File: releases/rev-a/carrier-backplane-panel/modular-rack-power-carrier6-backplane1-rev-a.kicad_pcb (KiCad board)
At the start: 4 copper layers, 163.8 x 237.3 mm, 723 parts

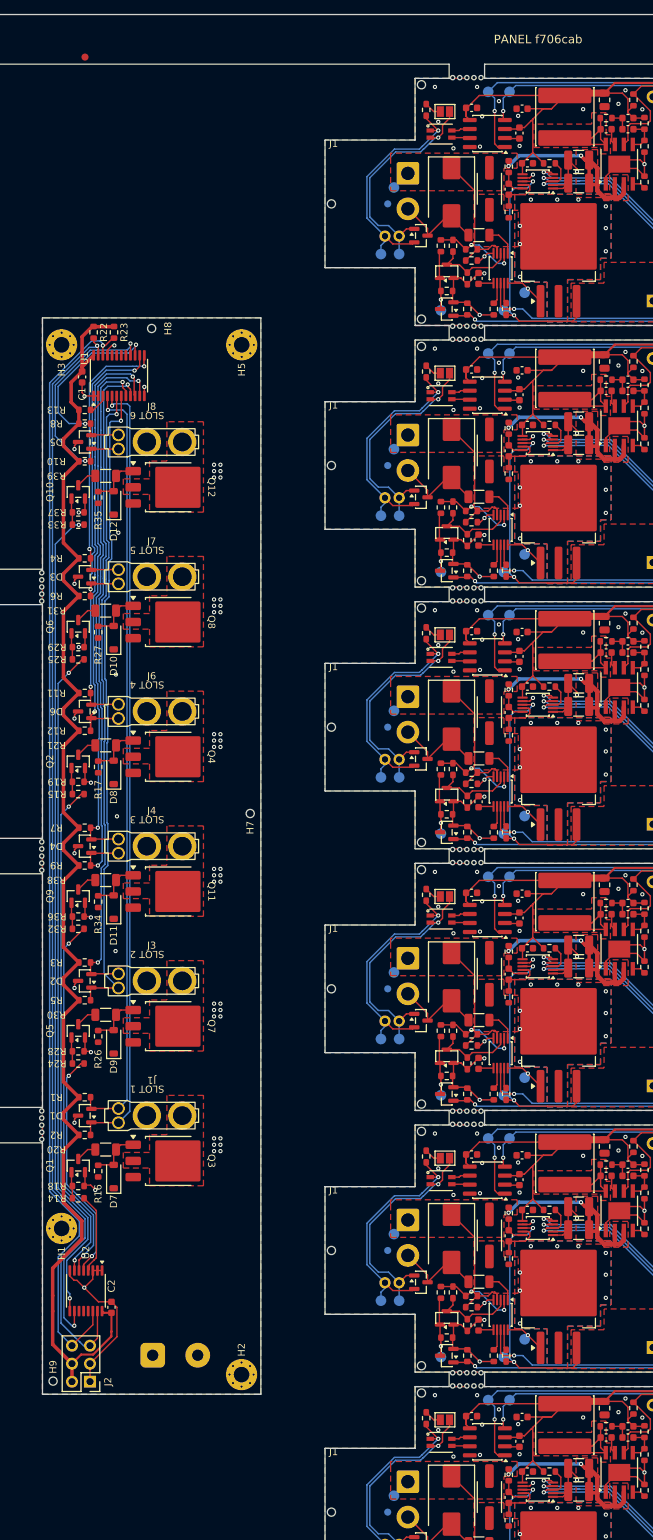
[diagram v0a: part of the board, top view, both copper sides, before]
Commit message: Gate panel builds and complete PCB renders
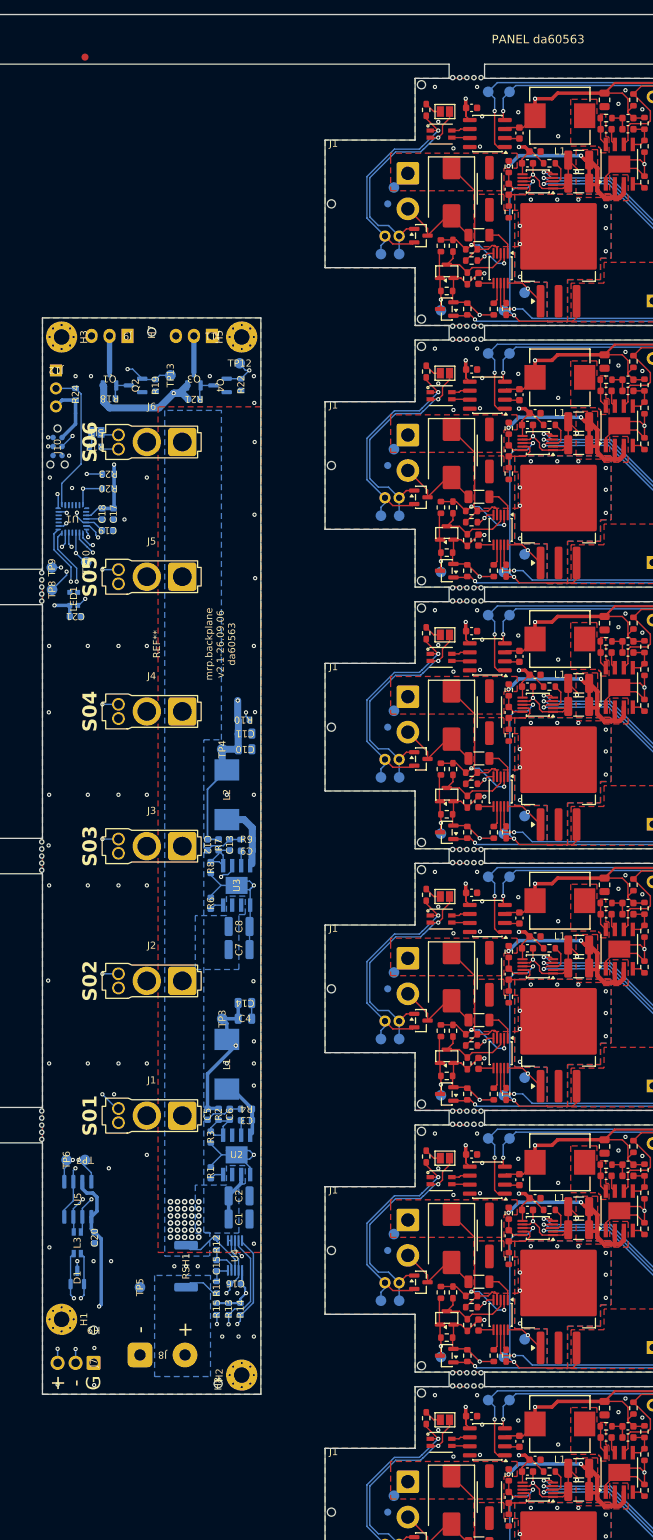
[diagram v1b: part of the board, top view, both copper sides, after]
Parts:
- removed BACKPLANE1-D10, BACKPLANE1-D11, BACKPLANE1-D12, BACKPLANE1-D7, BACKPLANE1-D8, BACKPLANE1-D9: BZT52C12-7-F, Diode_SMD:D_SOD-123
- removed BACKPLANE1-D2, BACKPLANE1-D3, BACKPLANE1-D4, BACKPLANE1-D5, BACKPLANE1-D6: PESD5V0S2BT,215, Package_TO_SOT_SMD:SOT-23
- removed BACKPLANE1-Q10, BACKPLANE1-Q5, BACKPLANE1-Q6, BACKPLANE1-Q9: BSS123, Package_TO_SOT_SMD:SOT-23
- removed BACKPLANE1-Q11, BACKPLANE1-Q12, BACKPLANE1-Q7, BACKPLANE1-Q8: SQD50P06-15L_GE3, Package_TO_SOT_SMD:TO-252-3_TabPin2
- removed BACKPLANE1-R16, BACKPLANE1-R26, BACKPLANE1-R27, BACKPLANE1-R34, BACKPLANE1-R35: 100k, Resistor_SMD:R_0603_1608Metric
- removed BACKPLANE1-R25, BACKPLANE1-R32, BACKPLANE1-R33: 1k, Resistor_SMD:R_0603_1608Metric
- removed BACKPLANE1-R28, BACKPLANE1-R29, BACKPLANE1-R36, BACKPLANE1-R37: 10k, Resistor_SMD:R_0603_1608Metric
- removed BACKPLANE1-R30, BACKPLANE1-R31, BACKPLANE1-R38, BACKPLANE1-R39: 10k, Resistor_SMD:R_1206_3216Metric
- removed BACKPLANE1-R5: 4.7k 1%, Resistor_SMD:R_0603_1608Metric
- removed the BACKPLANE1-REF** at (39.8, 76.0)
- added BACKPLANE1-C10: 22uF 25V, Capacitor_SMD:C_0805_2012Metric, B.Cu at (41.6, 104.6)
- added BACKPLANE1-C11: 22uF 25V, Capacitor_SMD:C_0805_2012Metric, B.Cu at (41.6, 102.4)
- added BACKPLANE1-C12: 3.3nF 50V X7R, Capacitor_SMD:C_0603_1608Metric, B.Cu at (36.3, 118.1)
- added BACKPLANE1-C13: 56pF 50V C0G, Capacitor_SMD:C_0603_1608Metric, B.Cu at (39.4, 118.1)
- added BACKPLANE1-C14: 22uF 25V, Capacitor_SMD:C_0805_2012Metric, B.Cu at (41.5, 140.4)
- added BACKPLANE1-C15: 100nF, Capacitor_SMD:C_0603_1608Metric, B.Cu at (37.6, 177.4)
- added BACKPLANE1-C16: 100nF, Capacitor_SMD:C_0603_1608Metric, B.Cu at (40.2, 180.0)
- added BACKPLANE1-C17: 100nF, Capacitor_SMD:C_0603_1608Metric, B.Cu at (23.0, 71.4)
- added BACKPLANE1-C18: 4.7uF, Capacitor_SMD:C_0603_1608Metric, B.Cu at (21.4, 71.4)
- added BACKPLANE1-C19: 100nF, Capacitor_SMD:C_0603_1608Metric, B.Cu at (22.2, 73.8)
- added BACKPLANE1-C20: 100nF, Capacitor_SMD:C_0603_1608Metric, B.Cu at (20.4, 173.5)
- added BACKPLANE1-C21: 100nF, Capacitor_SMD:C_0603_1608Metric, B.Cu at (17.6, 85.9)
- added BACKPLANE1-C3: 2.2nF 50V, Capacitor_SMD:C_0603_1608Metric, B.Cu at (41.8, 156.9)
- added BACKPLANE1-C4: 22uF 25V, Capacitor_SMD:C_0805_2012Metric, B.Cu at (41.5, 142.6)
- added BACKPLANE1-C5: 2.2nF 50V, Capacitor_SMD:C_0603_1608Metric, B.Cu at (36.3, 156.1)
- added BACKPLANE1-C6: 220pF C0G, Capacitor_SMD:C_0603_1608Metric, B.Cu at (39.4, 156.1)
- added BACKPLANE1-C7: 2.2uF 100V, Capacitor_SMD:C_1210_3225Metric, B.Cu at (40.7, 132.9)
- added BACKPLANE1-C8: 2.2uF 100V, Capacitor_SMD:C_1210_3225Metric, B.Cu at (40.7, 129.6)
- added BACKPLANE1-C9: 2.2nF 50V, Capacitor_SMD:C_0603_1608Metric, B.Cu at (41.8, 118.9)
- added BACKPLANE1-J10: SWD, Connector:Tag-Connect_TC2030-IDC-NL_2x03_P1.27mm_Vertical, B.Cu at (15.1, 61.9)
- added BACKPLANE1-J11: 12V 3-WIRE FAN, Connector_MiniRackPower:FanPinHeader_1x03_P2.54mm_Vertical_JLC_Edge, B.Cu at (36.9, 46.3)
- added BACKPLANE1-J12: DS18B20 EXT SUPPLY, Connector_PinHeader_2.54mm:PinHeader_1x03_P2.54mm_Vertical, B.Cu at (14.9, 51.2)
- added BACKPLANE1-J9: 12V 3-WIRE FAN, Connector_MiniRackPower:FanPinHeader_1x03_P2.54mm_Vertical_JLC_Edge, B.Cu at (25.0, 46.3)
- added BACKPLANE1-L1: 100uH, mini-rack-power:L_PRODTech_PSPMAA0805, B.Cu at (39.0, 149.0)
- added BACKPLANE1-L2: 100uH, mini-rack-power:L_PRODTech_PSPMAA0805, B.Cu at (39.0, 111.0)
- added BACKPLANE1-L3: ACT1210D-101-2P-TL00, mini-rack-power:L_CommonModeChoke_TDK_ACT1210D, B.Cu at (17.9, 174.2)
- added BACKPLANE1-LED1: WS2812B-2020-V6, LED_SMD:LED_WS2812B-2020_PLCC4_2.0x2.0mm, B.Cu at (17.4, 83.4)
- added BACKPLANE1-REF**: OSHW-Logo_11.4x12mm_SilkScreen, Symbol:OSHW-Logo_11.4x12mm_SilkScreen, B.Cu at (29.1, 89.8)
- added BACKPLANE1-RSH1: 1mR 1% 6W, Resistor_SMD:R_2512_6332Metric, B.Cu at (33.2, 177.5)
- added BACKPLANE1-SJ1: TERMINATION, Jumper:SolderJumper-2_P1.3mm_Open_Pad1.0x1.5mm, B.Cu at (20.6, 59.9)
- added BACKPLANE1-TP10: INA_ALERT, TestPoint:TestPoint_Pad_D1.5mm, B.Cu at (19.2, 78.2)
- added BACKPLANE1-TP12: FAN_PWM, TestPoint:TestPoint_Pad_D1.5mm, B.Cu at (40.8, 50.2)
- added BACKPLANE1-TP13: FAN_PWM, TestPoint:TestPoint_Pad_D1.5mm, B.Cu at (31.1, 51.9)
- added BACKPLANE1-TP3: +3V3, TestPoint:TestPoint_Pad_D1.5mm, B.Cu at (38.4, 142.6)
- added BACKPLANE1-TP4: +12V, TestPoint:TestPoint_Pad_D1.5mm, B.Cu at (38.4, 104.6)
- added BACKPLANE1-TP5: GND, TestPoint:TestPoint_Pad_D1.5mm, B.Cu at (26.8, 180.5)
- added BACKPLANE1-TP6: CAN_TX, TestPoint:TestPoint_Pad_D1.5mm, B.Cu at (16.4, 162.5)
- added BACKPLANE1-TP7: CAN_RX, TestPoint:TestPoint_Pad_D1.5mm, B.Cu at (19.0, 162.5)
- added BACKPLANE1-TP8: I2C_SDA, TestPoint:TestPoint_Pad_D1.5mm, B.Cu at (14.4, 82.1)
- added BACKPLANE1-TP9: I2C_SCL, TestPoint:TestPoint_Pad_D1.5mm, B.Cu at (14.3, 79.0)
- added BACKPLANE1-U3: LM5164DDAR, Package_SO:TI_SO-PowerPAD-8, B.Cu at (40.4, 123.8)
- added BACKPLANE1-U4: INA237AIDGSR, mini-rack-power:MSOP-10_3x3mm_P0.5mm_0.20mm_Clearance, B.Cu at (40.2, 176.0)
- added BACKPLANE1-U5: TCAN3413DR, Package_SO:SOIC-8_3.9x4.9mm_P1.27mm, B.Cu at (18.0, 168.1)
- BACKPLANE1-C1: value 100nF 100V -> 2.2uF 100V; footprint Capacitor_SMD:C_0603_1608Metric -> Capacitor_SMD:C_1210_3225Metric; moved to B.Cu
- BACKPLANE1-C2: value 100nF -> 2.2uF 100V; footprint Capacitor_SMD:C_0603_1608Metric -> Capacitor_SMD:C_1210_3225Metric; moved to B.Cu
- BACKPLANE1-D1: value PESD5V0S2BT,215 -> PESD2CANFD27V-TR; moved to B.Cu
- BACKPLANE1-H1, BACKPLANE1-H2, BACKPLANE1-H3, BACKPLANE1-H5: value MountingHole_Pad -> M2 CHASSIS
- BACKPLANE1-H7, BACKPLANE1-H8, BACKPLANE1-H9: moved to B.Cu
- BACKPLANE1-J1: value SLOT_1 -> XT30U_2+2
- BACKPLANE1-J2: value i2c_backpack -> XT30U_2+2; footprint Connector_PinHeader_2.54mm:PinHeader_2x03_P2.54mm_Vertical -> mini-rack-power:Amass_XT30U_2plus2_F
- BACKPLANE1-J3: value SLOT_2 -> XT30U_2+2
- BACKPLANE1-J4: value SLOT_3 -> XT30U_2+2
- BACKPLANE1-J5: value DC_IN -> XT30U_2+2; footprint mini-rack-power:DORABO_DB910-6.35-2P-GN-S -> mini-rack-power:Amass_XT30U_2plus2_F; moved to F.Cu
- BACKPLANE1-J6: value SLOT_4 -> XT30U_2+2
- BACKPLANE1-J7: value SLOT_5 -> XY308-2.54-3P / EXTERNAL CAN; footprint mini-rack-power:Amass_XT30U_2plus2_F -> mini-rack-power:TerminalBlock_Xinya_XY308-2.54-3P_1x03_P2.54mm_Horizontal; moved to B.Cu
- BACKPLANE1-J8: value SLOT_6 -> DC IN; footprint mini-rack-power:Amass_XT30U_2plus2_F -> mini-rack-power:DORABO_DB910-6.35-2P-GN-S; moved to B.Cu
- BACKPLANE1-Q1: value BSS123 -> AO3407A; moved to B.Cu
- BACKPLANE1-Q2: value BSS123 -> 2N7002; moved to B.Cu
- BACKPLANE1-Q3: value SQD50P06-15L_GE3 -> AO3407A; footprint Package_TO_SOT_SMD:TO-252-3_TabPin2 -> Package_TO_SOT_SMD:SOT-23; moved to B.Cu
- BACKPLANE1-Q4: value SQD50P06-15L_GE3 -> 2N7002; footprint Package_TO_SOT_SMD:TO-252-3_TabPin2 -> Package_TO_SOT_SMD:SOT-23; moved to B.Cu
- BACKPLANE1-R1: value 4.7k 1% -> 27k 1%; moved to B.Cu
- BACKPLANE1-R10, BACKPLANE1-R23: value 4.7k 1% -> 10k; moved to B.Cu
- BACKPLANE1-R11, BACKPLANE1-R12: value 4.7k 1% -> 10R; moved to B.Cu
- BACKPLANE1-R13: value 4.7k 1% -> 2.2k; moved to B.Cu
- BACKPLANE1-R14: value 1k -> 2.2k; moved to B.Cu
- BACKPLANE1-R15: value 1k -> 10k; moved to B.Cu
- BACKPLANE1-R17: value 100k -> 120R 1%; moved to B.Cu
- BACKPLANE1-R18, BACKPLANE1-R19: value 10k -> 100k 1%; moved to B.Cu
- BACKPLANE1-R2, BACKPLANE1-R4: value 4.7k 1% -> 110k 1%; moved to B.Cu
- BACKPLANE1-R20: footprint Resistor_SMD:R_1206_3216Metric -> Resistor_SMD:R_0603_1608Metric; moved to B.Cu
- BACKPLANE1-R21: value 10k -> 100k 1%; footprint Resistor_SMD:R_1206_3216Metric -> Resistor_SMD:R_0603_1608Metric; moved to B.Cu
- BACKPLANE1-R22, BACKPLANE1-R6: value 4.7k 1% -> 100k 1%; moved to B.Cu
- BACKPLANE1-R24: value 1k -> 4.7k 1%; moved to B.Cu
- BACKPLANE1-R3: value 4.7k 1% -> 62k 1%; moved to B.Cu
- BACKPLANE1-R7, BACKPLANE1-R9: value 4.7k 1% -> 453k 1%; moved to B.Cu
- BACKPLANE1-R8: value 4.7k 1% -> 49.9k 1%; moved to B.Cu
- BACKPLANE1-U1: value TCA9548APWR -> STM32C092GCU6; footprint Package_SO:TSSOP-24_4.4x7.8mm_P0.65mm -> Package_DFN_QFN:QFN-28_4x4mm_P0.5mm; moved to B.Cu
- BACKPLANE1-U2: value PCA9554PWR -> LM5164DDAR; footprint Package_SO:TSSOP-16_4.4x5mm_P0.65mm -> Package_SO:TI_SO-PowerPAD-8; moved to B.Cu
- CARRIER1-L1, CARRIER2-L1, CARRIER3-L1, CARRIER4-L1, CARRIER5-L1, CARRIER6-L1: value 68μH -> 100uH; footprint Inductor_SMD:L_Sunlord_SWPA8040S -> mini-rack-power:L_PRODTech_PSPMAA0805
- CARRIER1-U2, CARRIER2-U2, CARRIER3-U2, CARRIER4-U2, CARRIER5-U2, CARRIER6-U2: value LM5163DDAR -> LM5164DDAR
- moved BACKPLANE1-H8 149.1 mm to (37.8, 194.1), turned to -90 degrees
- moved BACKPLANE1-J8 128.8 mm to (29.9, 190.0)
- moved BACKPLANE1-R13 128.4 mm to (39.3, 183.5), turned to -90 degrees
- moved BACKPLANE1-C1 120.8 mm to (40.7, 170.9), turned to 0 degrees
- moved BACKPLANE1-J7 111.2 mm to (20.2, 191.2), turned to 180 degrees
- moved BACKPLANE1-R18 111.1 mm to (22.5, 55.2)
- moved BACKPLANE1-Q1 111.0 mm to (22.5, 52.4)
- moved BACKPLANE1-Q3 110.4 mm to (34.4, 52.4), turned to 90 degrees
- moved BACKPLANE1-J5 109.8 mm to (28.4, 80.3)
- moved BACKPLANE1-R24 94.4 mm to (17.7, 54.5), turned to 90 degrees
- moved BACKPLANE1-R20 93.2 mm to (22.3, 67.9)
- moved BACKPLANE1-R11 85.8 mm to (37.6, 180.5), turned to 90 degrees
- moved BACKPLANE1-R4 80.9 mm to (41.8, 155.3), turned to 180 degrees
- moved BACKPLANE1-R15 75.2 mm to (37.6, 183.5), turned to -90 degrees
- moved BACKPLANE1-R12 74.7 mm to (37.6, 174.4), turned to -90 degrees
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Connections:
- net BACKPLANE1-Net-(U1-SC6) renamed BACKPLANE1-unconnected-(U1-PA9/PA11-Pad18)
- net BACKPLANE1-Net-(U1-SD6) renamed BACKPLANE1-unconnected-(U1-PC6-Pad17)
- net BACKPLANE1-Net-(U1-SD7) renamed BACKPLANE1-unconnected-(U1-PA10/PA12-Pad19)
- BACKPLANE1-C1 pad 1: BACKPLANE1-+3V3 -> BACKPLANE1-VCC
- BACKPLANE1-C2 pad 1: BACKPLANE1-+3V3 -> BACKPLANE1-VCC
- BACKPLANE1-D1 pad 1: BACKPLANE1-SCL_SLOT_1 -> BACKPLANE1-/CAN-FD and Six Slots/CAN_EXT_N
- BACKPLANE1-D1 pad 2: BACKPLANE1-SDA_SLOT_1 -> BACKPLANE1-/CAN-FD and Six Slots/CAN_EXT_P
- BACKPLANE1-J1 pad 1: BACKPLANE1-GND -> BACKPLANE1-VCC
- BACKPLANE1-J1 pad 2: BACKPLANE1-SLOT_1_PWR_SW -> BACKPLANE1-GND
- BACKPLANE1-J1 pad 3: BACKPLANE1-SDA_SLOT_1 -> BACKPLANE1-/CAN-FD and Six Slots/CAN_BUS_P
- BACKPLANE1-J1 pad 4: BACKPLANE1-SCL_SLOT_1 -> BACKPLANE1-/CAN-FD and Six Slots/CAN_BUS_N
- BACKPLANE1-J2 pad 1: BACKPLANE1-GND -> BACKPLANE1-VCC
- BACKPLANE1-J2 pad 2: BACKPLANE1-+3V3 -> BACKPLANE1-GND
- BACKPLANE1-J2 pad 3: BACKPLANE1-GND -> BACKPLANE1-/CAN-FD and Six Slots/CAN_BUS_P
- BACKPLANE1-J2 pad 4: BACKPLANE1-+3V3 -> BACKPLANE1-/CAN-FD and Six Slots/CAN_BUS_N
- BACKPLANE1-J3 pad 1: BACKPLANE1-GND -> BACKPLANE1-VCC
- BACKPLANE1-J3 pad 2: BACKPLANE1-SLOT_2_PWR_SW -> BACKPLANE1-GND
- BACKPLANE1-J3 pad 3: BACKPLANE1-SDA_SLOT_2 -> BACKPLANE1-/CAN-FD and Six Slots/CAN_BUS_P
- BACKPLANE1-J3 pad 4: BACKPLANE1-SCL_SLOT_2 -> BACKPLANE1-/CAN-FD and Six Slots/CAN_BUS_N
- BACKPLANE1-J4 pad 1: BACKPLANE1-GND -> BACKPLANE1-VCC
- BACKPLANE1-J4 pad 2: BACKPLANE1-SLOT_3_PWR_SW -> BACKPLANE1-GND
- BACKPLANE1-J4 pad 3: BACKPLANE1-SDA_SLOT_3 -> BACKPLANE1-/CAN-FD and Six Slots/CAN_BUS_P
- BACKPLANE1-J4 pad 4: BACKPLANE1-SCL_SLOT_3 -> BACKPLANE1-/CAN-FD and Six Slots/CAN_BUS_N
- BACKPLANE1-J5 pad 1: BACKPLANE1-GND -> BACKPLANE1-VCC
- BACKPLANE1-J5 pad 2: BACKPLANE1-+24V -> BACKPLANE1-GND
- BACKPLANE1-J6 pad 1: BACKPLANE1-GND -> BACKPLANE1-VCC
- BACKPLANE1-J6 pad 2: BACKPLANE1-SLOT_4_PWR_SW -> BACKPLANE1-GND
- BACKPLANE1-J6 pad 3: BACKPLANE1-SDA_SLOT_4 -> BACKPLANE1-/CAN-FD and Six Slots/CAN_BUS_P
- BACKPLANE1-J6 pad 4: BACKPLANE1-SCL_SLOT_4 -> BACKPLANE1-/CAN-FD and Six Slots/CAN_BUS_N
- BACKPLANE1-J7 pad 2: BACKPLANE1-SLOT_5_PWR_SW -> BACKPLANE1-/CAN-FD and Six Slots/CAN_EXT_N
- BACKPLANE1-J7 pad 3: BACKPLANE1-SDA_SLOT_5 -> BACKPLANE1-/CAN-FD and Six Slots/CAN_EXT_P
- BACKPLANE1-J8 pad 2: BACKPLANE1-SLOT_6_PWR_SW -> BACKPLANE1-VIN_RAW
- BACKPLANE1-Q1 pad 2: BACKPLANE1-GND -> BACKPLANE1-+12V
- BACKPLANE1-Q1 pad 3: BACKPLANE1-Net-(Q1-D) -> BACKPLANE1-/Fan Control and Status/FAN_12V_SW
- BACKPLANE1-Q2 pad 1: BACKPLANE1-Net-(Q2-G) -> BACKPLANE1-FAN_PWM
- BACKPLANE1-Q2 pad 3: BACKPLANE1-Net-(Q2-D) -> BACKPLANE1-Net-(Q1-G)
- BACKPLANE1-Q3 pad 1: BACKPLANE1-Net-(D7-A) -> BACKPLANE1-Net-(Q3-G)
- BACKPLANE1-Q3 pad 2: BACKPLANE1-SLOT_1_PWR_SW -> BACKPLANE1-+12V
- BACKPLANE1-Q3 pad 3: BACKPLANE1-+24V -> BACKPLANE1-/Fan Control and Status/FAN2_12V_SW
- BACKPLANE1-Q4 pad 1: BACKPLANE1-Net-(D8-A) -> BACKPLANE1-FAN2_PWM
- BACKPLANE1-Q4 pad 2: BACKPLANE1-SLOT_4_PWR_SW -> BACKPLANE1-GND
- BACKPLANE1-Q4 pad 3: BACKPLANE1-+24V -> BACKPLANE1-Net-(Q3-G)
- BACKPLANE1-R1 pad 1: BACKPLANE1-+3V3 -> BACKPLANE1-Net-(U2-RON)
- BACKPLANE1-R1 pad 2: BACKPLANE1-SDA_SLOT_1 -> BACKPLANE1-GND
- BACKPLANE1-R10 pad 1: BACKPLANE1-+3V3 -> BACKPLANE1-+12V
- BACKPLANE1-R10 pad 2: BACKPLANE1-SCL_SLOT_6 -> BACKPLANE1-PGOOD_12V
- BACKPLANE1-R11 pad 1: BACKPLANE1-+3V3 -> BACKPLANE1-VIN_RAW
- BACKPLANE1-R11 pad 2: BACKPLANE1-SDA_SLOT_4 -> BACKPLANE1-/Power Input and Monitor/INA_IN_P
- BACKPLANE1-R12 pad 1: BACKPLANE1-+3V3 -> BACKPLANE1-VCC
- BACKPLANE1-R12 pad 2: BACKPLANE1-SCL_SLOT_4 -> BACKPLANE1-/Power Input and Monitor/INA_IN_N
- BACKPLANE1-R13 pad 2: BACKPLANE1-I2C_MUX_RESET_N -> BACKPLANE1-I2C_SDA
- BACKPLANE1-R14 pad 1: BACKPLANE1-SLOT_1_PWR_EN -> BACKPLANE1-+3V3
- BACKPLANE1-R14 pad 2: BACKPLANE1-Net-(Q1-G) -> BACKPLANE1-I2C_SCL
- BACKPLANE1-R15 pad 1: BACKPLANE1-SLOT_4_PWR_EN -> BACKPLANE1-+3V3
- BACKPLANE1-R15 pad 2: BACKPLANE1-Net-(Q2-G) -> BACKPLANE1-INA_ALERT
- BACKPLANE1-R17 pad 1: BACKPLANE1-+24V -> BACKPLANE1-Net-(SJ1-B)
- BACKPLANE1-R17 pad 2: BACKPLANE1-Net-(D8-A) -> BACKPLANE1-/CAN-FD and Six Slots/CAN_BUS_N
- BACKPLANE1-R18 pad 1: BACKPLANE1-Net-(Q1-G) -> BACKPLANE1-+12V
- BACKPLANE1-R18 pad 2: BACKPLANE1-GND -> BACKPLANE1-Net-(Q1-G)
- BACKPLANE1-R19 pad 1: BACKPLANE1-Net-(Q2-G) -> BACKPLANE1-FAN_PWM
- BACKPLANE1-R2 pad 2: BACKPLANE1-SCL_SLOT_1 -> BACKPLANE1-/Buck Converters/FB_3V3
- BACKPLANE1-R20 pad 1: BACKPLANE1-Net-(D7-A) -> BACKPLANE1-+3V3
- BACKPLANE1-R20 pad 2: BACKPLANE1-Net-(Q1-D) -> BACKPLANE1-FAN_TACH
- BACKPLANE1-R21 pad 1: BACKPLANE1-Net-(D8-A) -> BACKPLANE1-+12V
- BACKPLANE1-R21 pad 2: BACKPLANE1-Net-(Q2-D) -> BACKPLANE1-Net-(Q3-G)
- BACKPLANE1-R22 pad 1: BACKPLANE1-+3V3 -> BACKPLANE1-FAN2_PWM
- BACKPLANE1-R22 pad 2: BACKPLANE1-I2C_UP_SDA -> BACKPLANE1-GND
- BACKPLANE1-R23 pad 2: BACKPLANE1-I2C_UP_SCL -> BACKPLANE1-FAN2_TACH
- BACKPLANE1-R24 pad 1: BACKPLANE1-SLOT_2_PWR_EN -> BACKPLANE1-+3V3
- BACKPLANE1-R24 pad 2: BACKPLANE1-Net-(Q5-G) -> BACKPLANE1-DS18B20_DATA
- BACKPLANE1-R3 pad 1: BACKPLANE1-+3V3 -> BACKPLANE1-/Buck Converters/FB_3V3
- BACKPLANE1-R3 pad 2: BACKPLANE1-SDA_SLOT_2 -> BACKPLANE1-GND
- BACKPLANE1-R4 pad 1: BACKPLANE1-+3V3 -> BACKPLANE1-/Buck Converters/SW_3V3
- BACKPLANE1-R4 pad 2: BACKPLANE1-SDA_SLOT_5 -> BACKPLANE1-/Buck Converters/RIPPLE_3V3
- BACKPLANE1-R6 pad 1: BACKPLANE1-+3V3 -> BACKPLANE1-Net-(U3-RON)
- BACKPLANE1-R6 pad 2: BACKPLANE1-SCL_SLOT_5 -> BACKPLANE1-GND
- BACKPLANE1-R7 pad 1: BACKPLANE1-+3V3 -> BACKPLANE1-+12V
- BACKPLANE1-R7 pad 2: BACKPLANE1-SDA_SLOT_3 -> BACKPLANE1-/Buck Converters/FB_12V
- BACKPLANE1-R8 pad 1: BACKPLANE1-+3V3 -> BACKPLANE1-/Buck Converters/FB_12V
- BACKPLANE1-R8 pad 2: BACKPLANE1-SDA_SLOT_6 -> BACKPLANE1-GND
- BACKPLANE1-R9 pad 1: BACKPLANE1-+3V3 -> BACKPLANE1-/Buck Converters/SW_12V
- BACKPLANE1-R9 pad 2: BACKPLANE1-SCL_SLOT_3 -> BACKPLANE1-/Buck Converters/RIPPLE_12V
- BACKPLANE1-U1 pad 1: BACKPLANE1-GND -> BACKPLANE1-unconnected-(U1-PC14-Pad1)
- BACKPLANE1-U1 pad 10: BACKPLANE1-SDA_SLOT_4 -> BACKPLANE1-INA_ALERT
- BACKPLANE1-U1 pad 11: BACKPLANE1-SCL_SLOT_4 -> BACKPLANE1-unconnected-(U1-PA5-Pad11)
- BACKPLANE1-U1 pad 12: BACKPLANE1-GND -> BACKPLANE1-I2C_SDA
- BACKPLANE1-U1 pad 13: BACKPLANE1-SDA_SLOT_5 -> BACKPLANE1-I2C_SCL
- BACKPLANE1-U1 pad 14: BACKPLANE1-SCL_SLOT_5 -> BACKPLANE1-CAN_RX
- BACKPLANE1-U1 pad 15: BACKPLANE1-SDA_SLOT_6 -> BACKPLANE1-CAN_TX
- BACKPLANE1-U1 pad 16: BACKPLANE1-SCL_SLOT_6 -> BACKPLANE1-FAN2_TACH
- BACKPLANE1-U1 pad 2: BACKPLANE1-GND -> BACKPLANE1-unconnected-(U1-PC15-Pad2)
- BACKPLANE1-U1 pad 20: BACKPLANE1-Net-(U1-SC7) -> BACKPLANE1-/MCU and Local Control/SWDIO
- BACKPLANE1-U1 pad 21: BACKPLANE1-GND -> BACKPLANE1-/MCU and Local Control/SWCLK
- BACKPLANE1-U1 pad 22: BACKPLANE1-I2C_UP_SCL -> BACKPLANE1-DS18B20_DATA
- BACKPLANE1-U1 pad 23: BACKPLANE1-I2C_UP_SDA -> BACKPLANE1-unconnected-(U1-PB3-Pad23)
- BACKPLANE1-U1 pad 24: BACKPLANE1-+3V3 -> BACKPLANE1-unconnected-(U1-PB4-Pad24)
- BACKPLANE1-U1 pad 3: BACKPLANE1-I2C_MUX_RESET_N -> BACKPLANE1-+3V3
- BACKPLANE1-U1 pad 4: BACKPLANE1-SDA_SLOT_1 -> BACKPLANE1-GND
- BACKPLANE1-U1 pad 5: BACKPLANE1-SCL_SLOT_1 -> BACKPLANE1-/MCU and Local Control/NRST
- BACKPLANE1-U1 pad 6: BACKPLANE1-SDA_SLOT_2 -> BACKPLANE1-FAN2_PWM
- BACKPLANE1-U1 pad 7: BACKPLANE1-SCL_SLOT_2 -> BACKPLANE1-/MCU and Local Control/LED_DATA_RAW
- BACKPLANE1-U1 pad 8: BACKPLANE1-SDA_SLOT_3 -> BACKPLANE1-FAN_PWM
- BACKPLANE1-U1 pad 9: BACKPLANE1-SCL_SLOT_3 -> BACKPLANE1-PGOOD_12V
- BACKPLANE1-U2 pad 2: BACKPLANE1-GND -> BACKPLANE1-VCC
- BACKPLANE1-U2 pad 3: BACKPLANE1-GND -> BACKPLANE1-VCC
- BACKPLANE1-U2 pad 4: BACKPLANE1-SLOT_1_PWR_EN -> BACKPLANE1-Net-(U2-RON)
- BACKPLANE1-U2 pad 5: BACKPLANE1-SLOT_2_PWR_EN -> BACKPLANE1-/Buck Converters/FB_3V3
- BACKPLANE1-U2 pad 6: BACKPLANE1-SLOT_3_PWR_EN -> BACKPLANE1-unconnected-(U2-PGOOD-Pad6)
- BACKPLANE1-U2 pad 7: BACKPLANE1-SLOT_4_PWR_EN -> BACKPLANE1-/Buck Converters/BST_3V3
- BACKPLANE1-U2 pad 8: BACKPLANE1-GND -> BACKPLANE1-/Buck Converters/SW_3V3
- BACKPLANE1-U2 pad 9: BACKPLANE1-SLOT_5_PWR_EN -> BACKPLANE1-GND
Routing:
- net BACKPLANE1-I2C_SDA: track 0.00 -> 160.9 mm, vias 0 -> 3
- net BACKPLANE1-I2C_UP_SCL: track 159.5 -> 0.00 mm, vias 1 -> 0
- net BACKPLANE1-I2C_SCL: track 0.00 -> 159.2 mm, vias 0 -> 3
- net BACKPLANE1-INA_ALERT: track 0.00 -> 158.0 mm, vias 0 -> 3
- net BACKPLANE1-I2C_UP_SDA: track 157.6 -> 0.00 mm, vias 1 -> 0
- net BACKPLANE1-/CAN-FD and Six Slots/CAN_BUS_P: track 0.00 -> 132.4 mm, vias 0 -> 6
- net BACKPLANE1-/CAN-FD and Six Slots/CAN_BUS_N: track 0.00 -> 125.7 mm, vias 0 -> 2
- net BACKPLANE1-SLOT_6_PWR_EN: track 121.3 -> 0.00 mm, vias 2 -> 0
- net BACKPLANE1-PGOOD_12V: track 0.00 -> 117.1 mm, vias 0 -> 3
- net BACKPLANE1-SCL_SLOT_1: track 111.5 -> 0.00 mm, vias 1 -> 0
- net BACKPLANE1-SDA_SLOT_1: track 108.9 -> 0.00 mm, vias 1 -> 0
- net BACKPLANE1-SLOT_5_PWR_EN: track 96.7 -> 0.00 mm, vias 2 -> 0
- net BACKPLANE1-+3V3: track 192.1 -> 287.9 mm, vias 0 -> 5
- net BACKPLANE1-CAN_RX: track 0.00 -> 94.3 mm, vias 0 -> 2
- net BACKPLANE1-CAN_TX: track 0.00 -> 94.0 mm, vias 0 -> 2
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- added copper zone on F.Cu, net BACKPLANE1-GND
- added copper zone on In2.Cu, net BACKPLANE1-GND
- added copper zone on B.Cu, net BACKPLANE1-VCC
- added copper zone on F.Cu, net BACKPLANE1-VCC
- added copper zone on In1.Cu, net BACKPLANE1-VCC
- added copper zone on In2.Cu, net BACKPLANE1-VCC
- added copper zone on B.Cu, net BACKPLANE1-VIN_RAW
- added copper zone on In1.Cu, net CARRIER1-/Protected Power and Controls/HS_SENSE
- added copper zone on In2.Cu, net CARRIER1-/Protected Power and Controls/HS_SENSE
- added copper zone on In1.Cu, net CARRIER2-/Protected Power and Controls/HS_SENSE
- added copper zone on In2.Cu, net CARRIER2-/Protected Power and Controls/HS_SENSE
- added copper zone on In1.Cu, net CARRIER3-/Protected Power and Controls/HS_SENSE
- added copper zone on In2.Cu, net CARRIER3-/Protected Power and Controls/HS_SENSE
- added copper zone on In1.Cu, net CARRIER4-/Protected Power and Controls/HS_SENSE
- added copper zone on In2.Cu, net CARRIER4-/Protected Power and Controls/HS_SENSE
- added copper zone on In1.Cu, net CARRIER5-/Protected Power and Controls/HS_SENSE
- added copper zone on In2.Cu, net CARRIER5-/Protected Power and Controls/HS_SENSE
- added copper zone on In1.Cu, net CARRIER6-/Protected Power and Controls/HS_SENSE
- added copper zone on In2.Cu, net CARRIER6-/Protected Power and Controls/HS_SENSE
- removed copper zone on F.Cu, net BACKPLANE1-+24V
- removed copper zone on In2.Cu, net BACKPLANE1-+24V
- removed copper zone on F.Cu, net BACKPLANE1-SLOT_1_PWR_SW
- removed copper zone on F.Cu, net BACKPLANE1-SLOT_2_PWR_SW
- removed copper zone on F.Cu, net BACKPLANE1-SLOT_3_PWR_SW
- removed copper zone on F.Cu, net BACKPLANE1-SLOT_4_PWR_SW
- removed copper zone on F.Cu, net BACKPLANE1-SLOT_5_PWR_SW
- removed copper zone on F.Cu, net BACKPLANE1-SLOT_6_PWR_SW
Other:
- board text added: "+"
- board text added: "-"
- board text added: "12V"
- board text added: "3v3"
- board text added: "ALRT"
- board text added: "C19"
- board text added: "C20"
- board text added: "C21"
- board text added: "F1_PWM"
- board text added: "F2_PWM"
- board text added: "G"
- board text added: "J10"
- board text added: "J11"
- board text added: "J12"
- board text added: "J9"
- board text added: "L2"
- board text added: "PANEL da60563"
- board text added: "RSH1"
- board text added: "RX"
- board text added: "S01"
- board text added: "S02"
- board text added: "S03"
- board text added: "S04"
- board text added: "S05"
- board text added: "S06"
- board text added: "TP10"
- board text added: "TP12"
- board text added: "TP13"
- board text added: "TP3"
- board text added: "TP4"
- board text added: "TP8"
- board text added: "TP9"
- board text added: "TX"
- board text added: "VIN"
- board text added: "mrp.backplane v2.1-26.09.06 da60563"
- board text added: "mrp.carrier v2.1-26.09.06 da60563"
- board text removed: "+24V"
- board text removed: "BP.m2v1 26.08.16"
- board text removed: "D10"
- board text removed: "D11"
- board text removed: "D12"
- board text removed: "D3"
- board text removed: "D4"
- board text removed: "D5"
- board text removed: "D6"
- board text removed: "D7"
- board text removed: "D8"
- board text removed: "D9"
- board text removed: "PANEL f706cab"
- board text removed: "PD-CARRIER M2v1.26.08.29"
- board text removed: "Q10"
- board text removed: "Q11"
- board text removed: "Q12"
- board text removed: "Q5"
- board text removed: "Q6"
- board text removed: "Q7"
- board text removed: "Q8"
- board text removed: "Q9"
- board text removed: "R27"
- board text removed: "R29"
- board text removed: "R33"
- board text removed: "R34"
- board text removed: "R35"
- board text removed: "R36"
- board text removed: "R37"
- board text removed: "R38"
- board text removed: "R39"
- board text removed: "SLOT 1"
- board text removed: "SLOT 2"
- board text removed: "SLOT 3"
- board text removed: "SLOT 4"
- board text removed: "SLOT 5"
- board text removed: "SLOT 6"
